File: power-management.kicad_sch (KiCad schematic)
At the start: 11 parts, among them Q1 PMOS, U4 AP2112K-3.3

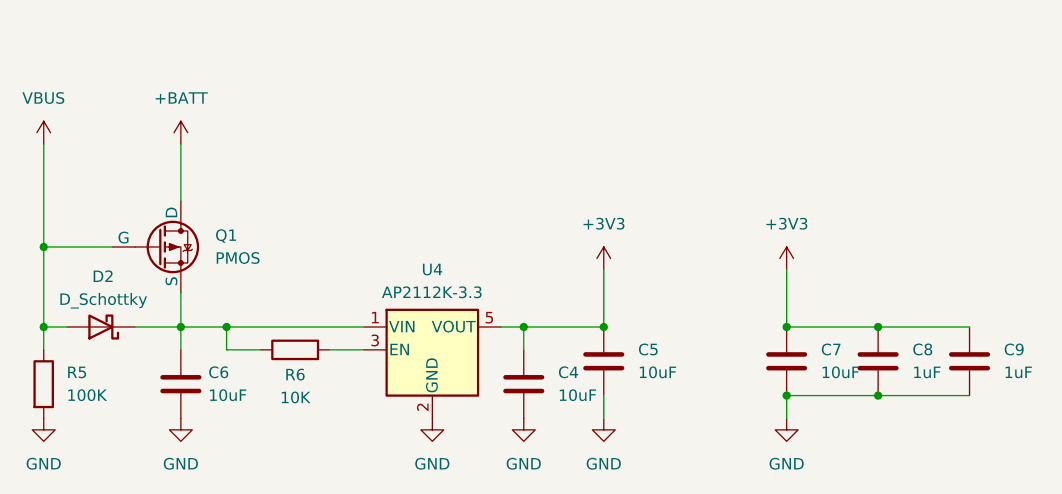
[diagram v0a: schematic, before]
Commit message: Adding symbols information
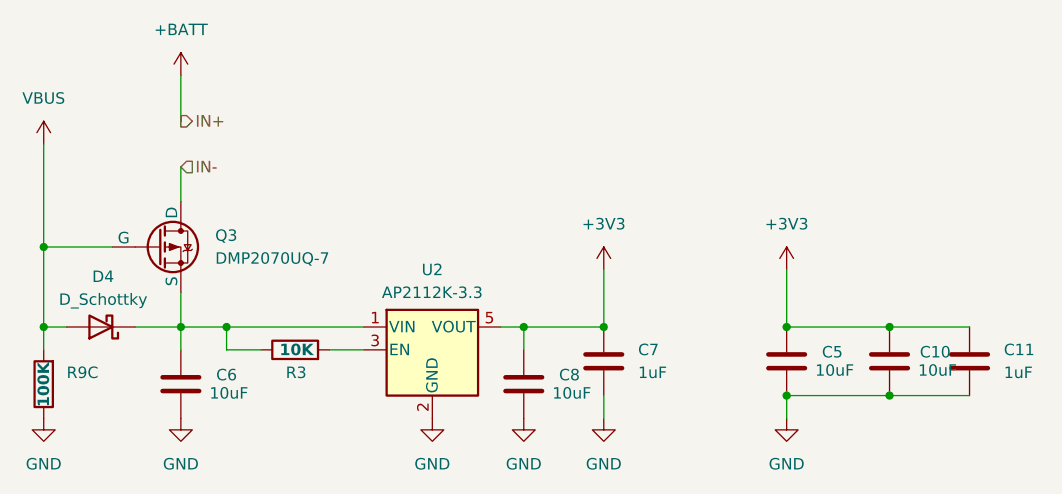
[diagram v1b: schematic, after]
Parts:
- removed C4: 10uF, symbol Device:C
- removed C9: 1uF, symbol Device:C
- removed R5: 100K, symbol Device:R
- removed R6: 10K, symbol Device:R
- added C10: 10uF, Inductor_SMD:L_0805_2012Metric, symbol Device:C
- added C11: 1uF, Capacitor_SMD:C_0603_1608Metric, symbol Device:C
- added R3: 10K, Resistor_SMD:R_0603_1608Metric, symbol Device:R
- added R9C: 100K, Resistor_SMD:R_Array_Convex_4x1206, symbol Device:R
- C5, C6: footprint (none) -> Inductor_SMD:L_0805_2012Metric; Mfr (none) -> Samsung Electro-Mechanics; Mfr P/N (none) -> CL21A106KOQNNNE; Supplier_1 (none) -> Digikey; Supplier_1 P/N (none) -> 1276-1096-1-ND; Supplier_1 Price @ Qty (none) -> 0.03130; Supplier_1 Unit Price (none) -> 0.10
- C7: value 10uF -> 1uF; footprint (none) -> Capacitor_SMD:C_0603_1608Metric; Mfr (none) -> YAGEO; Mfr P/N (none) -> CC0603KRX7R7BB105; Supplier_1 (none) -> Digikey; Supplier_1 P/N (none) -> 0.10; Supplier_1 Unit Price (none) -> 0.03080
- C8: value 1uF -> 10uF; footprint (none) -> Inductor_SMD:L_0805_2012Metric; Mfr (none) -> Samsung Electro-Mechanics; Mfr P/N (none) -> CL21A106KOQNNNE; Supplier_1 (none) -> Digikey; Supplier_1 P/N (none) -> 1276-1096-1-ND; Supplier_1 Price @ Qty (none) -> 0.03130; Supplier_1 Unit Price (none) -> 0.10
- Q3: renamed from Q1; value PMOS -> DMP2070UQ-7; footprint (none) -> Package_TO_SOT_SMD:SOT-23-5_HandSoldering; Mfr (none) -> Diodes Incorporated; Mfr P/N (none) -> DMP2070UQ-7; Supplier_1 (none) -> Digikey; Supplier_1 P/N (none) -> 31-DMP2070UQ-7CT-ND; Supplier_1 Price @ Qty (none) -> 0.1860; Supplier_1 Unit Price (none) -> 0.48
- U2: renamed from U4; Mfr (none) -> Diodes Incorporated; Mfr P/N (none) -> AP2112K-3.3TRG1; Supplier_1 (none) -> Digikey; Supplier_1 P/N (none) -> AP2112K-3.3TRG1DICT-ND; Supplier_1 Price @ Qty (none) -> 0.1955; Supplier_1 Unit Price (none) -> 0.35
- renumbered D2 to D4
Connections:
- net +3V3: now also C10.1, C11.2
- net +BATT: no longer Q3.1 (D)
- net GND: now also C10.2, C11.1, R9C.1
- net VBUS: now also R9C.2
- net at C6.1, D4.1 (K), Q3.3 (S)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: now also R3.1
- net at U2.3 (EN): now also R3.2
- new net IN-: Q3.1 (D)
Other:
- company: (none) -> catbranchman
- title: (none) -> Power - Management

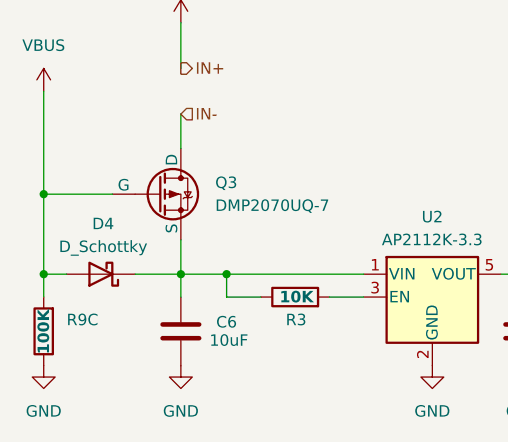
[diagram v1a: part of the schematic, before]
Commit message: Fixing footprint imports
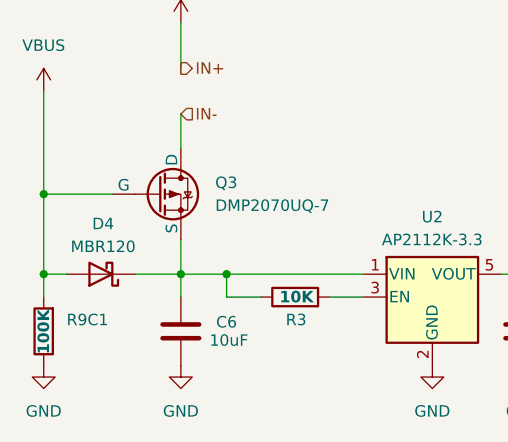
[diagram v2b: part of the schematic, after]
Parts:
- removed R9C: 100K, Resistor_SMD:R_Array_Convex_4x1206, symbol Device:R
- added R9C1: 100K, Resistor_SMD:R_Array_Convex_4x0603, symbol Device:R
- D4: value D_Schottky -> MBR120; footprint (none) -> Diode_SMD:D_SOD-123; Mfr (none) -> onsemi; Mfr P/N (none) -> MBR120LSFT1G; Supplier_1 (none) -> Digikey; Supplier_1 P/N (none) -> MBR120LSFT1GOSCT-ND; Supplier_1 Price @ Qty (none) -> 0.19610; Supplier_1 Unit Price (none) -> 0.42
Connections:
- net GND: now also R9C1.1
- net VBUS: now also R9C1.2
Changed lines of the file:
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@@
 			)
 		)
-		(property "Value" "D_Schottky"
+		(property "Value" "MBR120"
 			(at 87.884 102.362 0)
 			(effects
@@
 			)
 		)
-		(property "Footprint" ""
+		(property "Footprint" "Diode_SMD:D_SOD-123"
 			(at 87.63 105.41 0)
 			(effects
@@
 			)
 		)
-		(property "Datasheet" "~"
+		(property "Datasheet" "https://www.onsemi.com/pdf/datasheet/mbr120lsft1-d.pdf"
 			(at 87.63 105.41 0)
 			(effects
@@
 			)
 		)
-		(property "Description" "Schottky diode"
+		(property "Description" "Diode 20 V 1A Surface Mount SOD-123FL"
+			(at 87.63 105.41 0)
+			(effects
+				(font
+					(size 1.27 1.27)
+				)
+				(hide yes)
+			)
+		)
+		(property "Mfr" "onsemi"
+			(at 87.63 105.41 0)
+			(effects
+				(font
+					(size 1.27 1.27)
+				)
+				(hide yes)
+			)
+		)
+		(property "Mfr P/N" "MBR120LSFT1G"
+			(at 87.63 105.41 0)
+			(effects
+				(font
+					(size 1.27 1.27)
+				)
+				(hide yes)
+			)
+		)
+		(property "Supplier_1" "Digikey"
+			(at 87.63 105.41 0)
+			(effects
+				(font
+					(size 1.27 1.27)
+				)
+				(hide yes)
+			)
+		)
+		(property "Supplier_1 P/N" "MBR120LSFT1GOSCT-ND"
+			(at 87.63 105.41 0)
+			(effects
+				(font
+					(size 1.27 1.27)
+				)
+				(hide yes)
+			)
+		)
+		(property "Supplier_1 Unit Price" "0.42"
+			(at 87.63 105.41 0)
+			(effects
+				(font
+					(size 1.27 1.27)
+				)
+				(hide yes)
+			)
+		)
+		(property "Supplier_1 Price @ Qty" "0.19610"
+			(at 87.63 105.41 0)
+			(effects
+				(font
+					(size 1.27 1.27)
+				)
+				(hide yes)
+			)
+		)
+		(property "Supplier_2" ""
+			(at 87.63 105.41 0)
+			(effects
+				(font
+					(size 1.27 1.27)
+				)
+				(hide yes)
+			)
+		)
+		(property "Supplier_2 P/N" ""
+			(at 87.63 105.41 0)
+			(effects
+				(font
+					(size 1.27 1.27)
+				)
+				(hide yes)
+			)
+		)
+		(property "Supplier_2 Unit Price" ""
+			(at 87.63 105.41 0)
+			(effects
+				(font
+					(size 1.27 1.27)
+				)
+				(hide yes)
+			)
+		)
+		(property "Supplier_2 Price @ Qty" ""
 			(at 87.63 105.41 0)
 			(effects
@@
 	)
 	(symbol
+		(lib_id "Device:R")
+		(at 81.28 111.76 180)
+		(unit 1)
+		(exclude_from_sim no)
+		(in_bom yes)
+		(on_board yes)
+		(dnp no)
+		(property "Reference" "R9C1"
+			(at 83.82 110.4899 0)
+			(effects
+				(font
+					(size 1.27 1.27)
+				)
+				(justify right)
+			)
+		)
+		(property "Value" "100K"
+			(at 81.28 114.3 90)
+			(effects
+				(font
+					(size 1.27 1.27)
+					(thickness 0.254)
+					(bold yes)
+				)
+				(justify right)
+			)
+		)
+		(property "Footprint" "Resistor_SMD:R_Array_Convex_4x0603"
+			(at 83.058 111.76 90)
+			(effects
+				(font
+					(size 1.27 1.27)
+				)
+				(hide yes)
+			)
+		)
+		(property "Datasheet" "https://www.bourns.com/docs/Product-Datasheets/CATCAY.pdf"
+			(at 81.28 111.76 0)
+			(effects
+				(font
+					(size 1.27 1.27)
+				)
+				(hide yes)
+			)
+		)
+		(property "Description" "100k Ohm 1% 62.5mW Power Per Element Isolated 4 Resistor Network/Array 200pm/°C 1206 (3216 Metric), Convex, Long Side Terminals."
+			(at 81.28 111.76 0)
+			(effects
+				(font
+					(size 1.27 1.27)
+				)
+				(hide yes)
+			)
+		)
+		(property "Mfr" "Bourns Inc."
+			(at 81.28 111.76 0)
+			(effects
+				(font
+					(size 1.27 1.27)
+				)
+				(hide yes)
+			)
+		)
+		(property "Mfr P/N" "CAY16-1003F4LF"
+			(at 81.28 111.76 0)
+			(effects
+				(font
+					(size 1.27 1.27)
+				)
+				(hide yes)
+			)
+		)
+		(property "Supplier_1" "Digikey"
+			(at 81.28 111.76 0)
+			(effects
+				(font
+					(size 1.27 1.27)
+				)
+				(hide yes)
+			)
+		)
+		(property "Supplier_1 P/N" "CAY16-1003F4LFCT-ND"
+			(at 81.28 111.76 0)
+			(effects
+				(font
+					(size 1.27 1.27)
+				)
+				(hide yes)
+			)
+		)
+		(property "Supplier_1 Unit Price" "0.10"
+			(at 81.28 111.76 0)
+			(effects
+				(font
+					(size 1.27 1.27)
+				)
+				(hide yes)
+			)
+		)
+		(property "Supplier_1 Price @ Qty" "0.03170"
+			(at 81.28 111.76 0)
+			(effects
+				(font
+					(size 1.27 1.27)
+				)
+				(hide yes)
+			)
+		)
+		(property "Supplier_2" ""
+			(at 81.28 111.76 0)
+			(effects
+				(font
+					(size 1.27 1.27)
+				)
+				(hide yes)
+			)
+		)
+		(property "Supplier_2 P/N" ""
+			(at 81.28 111.76 0)
+			(effects
+				(font
+					(size 1.27 1.27)
+				)
+				(hide yes)
+			)
+		)
+		(property "Supplier_2 Unit Price" ""
+			(at 81.28 111.76 0)
+			(effects
+				(font
+					(size 1.27 1.27)
+				)
+				(hide yes)
+			)
+		)
+		(property "Supplier_2 Price @ Qty" ""
+			(at 81.28 111.76 0)
+			(effects
+				(font
+					(size 1.27 1.27)
+				)
+				(hide yes)
+			)
+		)
+		(pin "2"
+		)
+		(pin "1"
+		)
+		(instances
+			(project "roamer"
+				(path "/1c59de6a-87fe-4223-8898-4b0383164a31/f8947920-db82-4e9f-9d4f-25a180fcfca7"
+					(reference "R9C1")
+					(unit 1)
+				)
+			)
+		)
+	)
+	(symbol
 		(lib_id "Regulator_Linear:AP2112K-3.3")
 		(at 124.46 107.95 0)
@@
 					(unit 1)
 				)
-			)
-		)
-	)
-	(symbol
-		(lib_id "Device:R")
-		(at 81.28 111.76 180)
-		(unit 1)
-		(exclude_from_sim no)
-		(in_bom yes)
-		(on_board yes)
-		(dnp no)
-		(property "Reference" "R9C"
-			(at 83.82 110.4899 0)
-			(effects
-				(font
-					(size 1.27 1.27)
-				)
-				(justify right)
-			)
-		)
-		(property "Value" "100K"
-			(at 81.28 114.3 90)
-			(effects
-				(font
-					(size 1.27 1.27)
-					(thickness 0.254)
-					(bold yes)
-				)
-				(justify right)
-			)
-		)
-		(property "Footprint" "Resistor_SMD:R_Array_Convex_4x1206"
-			(at 83.058 111.76 90)
-			(effects
-				(font
-					(size 1.27 1.27)
-				)
-				(hide yes)
-			)
-		)
-		(property "Datasheet" "https://www.bourns.com/docs/Product-Datasheets/CATCAY.pdf"
-			(at 81.28 111.76 0)
-			(effects
-				(font
-					(size 1.27 1.27)
-				)
-				(hide yes)
-			)
-		)
-		(property "Description" "100k Ohm 1% 62.5mW Power Per Element Isolated 4 Resistor Network/Array 200pm/°C 1206 (3216 Metric), Convex, Long Side Terminals."
-			(at 81.28 111.76 0)
-			(effects
-				(font
-					(size 1.27 1.27)
-				)
-				(hide yes)
-			)
-		)
-		(property "Mfr" "Bourns Inc."
-			(at 81.28 111.76 0)
-			(effects
-				(font
-					(size 1.27 1.27)
-				)
-				(hide yes)
-			)
-		)
-		(property "Mfr P/N" "CAY16-1003F4LF"
-			(at 81.28 111.76 0)
-			(effects
-				(font
-					(size 1.27 1.27)
-				)
-				(hide yes)
-			)
-		)
-		(property "Supplier_1" "Digikey"
-			(at 81.28 111.76 0)
-			(effects
-				(font
-					(size 1.27 1.27)
-				)
-				(hide yes)
-			)
-		)
-		(property "Supplier_1 P/N" "CAY16-1003F4LFCT-ND"
-			(at 81.28 111.76 0)
-			(effects
-				(font
-					(size 1.27 1.27)
-				)
-				(hide yes)
-			)
-		)
-		(property "Supplier_1 Unit Price" "0.10"
-			(at 81.28 111.76 0)
-			(effects
-				(font
-					(size 1.27 1.27)
-				)
-				(hide yes)
-			)
-		)
-		(property "Supplier_1 Price @ Qty" "0.03170"
-			(at 81.28 111.76 0)
-			(effects
-				(font
-					(size 1.27 1.27)
-				)
-				(hide yes)
-			)
-		)
-		(property "Supplier_2" ""
-			(at 81.28 111.76 0)
-			(effects
-				(font
-					(size 1.27 1.27)
-				)
-				(hide yes)
-			)
-		)
-		(property "Supplier_2 P/N" ""
-			(at 81.28 111.76 0)
-			(effects
-				(font
-					(size 1.27 1.27)
-				)
-				(hide yes)
-			)
-		)
-		(property "Supplier_2 Unit Price" ""
-			(at 81.28 111.76 0)
-			(effects
-				(font
-					(size 1.27 1.27)
-				)
-				(hide yes)
-			)
-		)
-		(property "Supplier_2 Price @ Qty" ""
-			(at 81.28 111.76 0)
-			(effects
-				(font
-					(size 1.27 1.27)
-				)
-				(hide yes)
-			)
-		)
-		(pin "2"
-		)
-		(pin "1"
-		)
-		(instances
-			(project "roamer"
-				(path "/1c59de6a-87fe-4223-8898-4b0383164a31/f8947920-db82-4e9f-9d4f-25a180fcfca7"
-					(reference "R9C")
-					(unit 1)
-				)

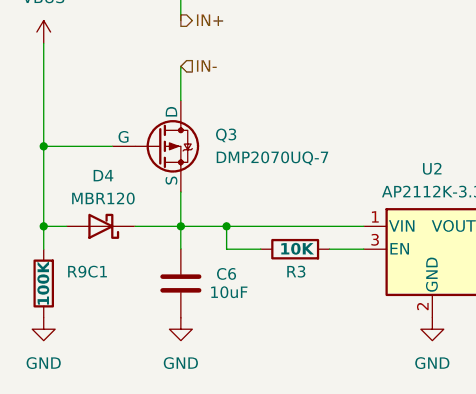
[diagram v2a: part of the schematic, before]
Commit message: Spamming 0 ohm resistors
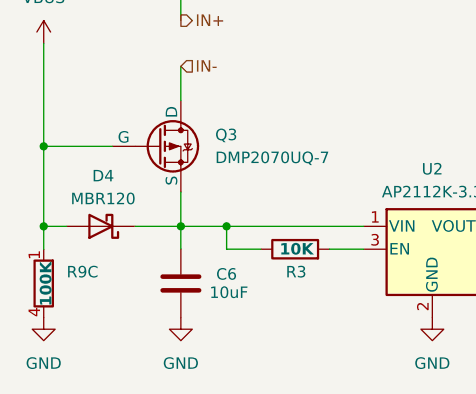
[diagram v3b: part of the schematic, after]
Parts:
- removed R9C1: 100K, Resistor_SMD:R_Array_Convex_4x0603, symbol Device:R
- added R9: 100K, Resistor_SMD:R_Array_Convex_4x1206, symbol Device:R_Network04_Split
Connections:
- net GND: now also R9.4 (R3.2)
- net VBUS: now also R9.1 (R1)
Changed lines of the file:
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@@
+	)
+	(symbol
+		(lib_id "Device:R_Network04_Split")
+		(at 81.28 111.76 0)
+		(unit 3)
+		(exclude_from_sim no)
+		(in_bom yes)
+		(on_board yes)
+		(dnp no)
+		(property "Reference" "R9"
+			(at 83.82 110.4899 0)
+			(effects
+				(font
+					(size 1.27 1.27)
+				)
+				(justify left)
+			)
+		)
+		(property "Value" "100K"
+			(at 81.534 114.3 90)
+			(effects
+				(font
+					(size 1.27 1.27)
+					(thickness 0.254)
+					(bold yes)
+				)
+				(justify left)
+			)
+		)
+		(property "Footprint" "Resistor_SMD:R_Array_Convex_4x1206"
+			(at 79.248 111.76 90)
+			(effects
+				(font
+					(size 1.27 1.27)
+				)
+				(hide yes)
+			)
+		)
+		(property "Datasheet" "https://www.bourns.com/docs/Product-Datasheets/CATCAY.pdf"
+			(at 81.28 111.76 0)
+			(effects
+				(font
+					(size 1.27 1.27)
+				)
+				(hide yes)
+			)
+		)
+		(property "Description" "100k Ohm 1% 62.5mW Power Per Element Isolated 4 Resistor Network/Array 200pm/°C 1206 (3216 Metric), Convex, Long Side Terminals."
+			(at 81.28 111.76 0)
+			(effects
+				(font
+					(size 1.27 1.27)
+				)
+				(hide yes)
+			)
+		)
+		(property "Mfr" "Bourns Inc."
+			(at 81.28 111.76 0)
+			(effects
+				(font
+					(size 1.27 1.27)
+				)
+				(hide yes)
+			)
+		)
+		(property "Mfr P/N" "CAY16-1003F4LF"
+			(at 81.28 111.76 0)
+			(effects
+				(font
+					(size 1.27 1.27)
+				)
+				(hide yes)
+			)
+		)
+		(property "Supplier_1" "Digikey"
+			(at 81.28 111.76 0)
+			(effects
+				(font
+					(size 1.27 1.27)
+				)
+				(hide yes)
+			)
+		)
+		(property "Supplier_1 P/N" "CAY16-1003F4LFCT-ND"
+			(at 81.28 111.76 0)
+			(effects
+				(font
+					(size 1.27 1.27)
+				)
+				(hide yes)
+			)
+		)
+		(property "Supplier_1 Unit Price" "0.10"
+			(at 81.28 111.76 0)
+			(effects
+				(font
+					(size 1.27 1.27)
+				)
+				(hide yes)
+			)
+		)
+		(property "Supplier_1 Price @ Qty" "0.03170"
+			(at 81.28 111.76 0)
+			(effects
+				(font
+					(size 1.27 1.27)
+				)
+				(hide yes)
+			)
+		)
+		(property "Supplier_2" ""
+			(at 81.28 111.76 0)
+			(effects
+				(font
+					(size 1.27 1.27)
+				)
+				(hide yes)
+			)
+		)
+		(property "Supplier_2 P/N" ""
+			(at 81.28 111.76 0)
+			(effects
+				(font
+					(size 1.27 1.27)
+				)
+				(hide yes)
+			)
+		)
+		(property "Supplier_2 Unit Price" ""
+			(at 81.28 111.76 0)
+			(effects
+				(font
+					(size 1.27 1.27)
+				)
+				(hide yes)
+			)
+		)
+		(property "Supplier_2 Price @ Qty" ""
+			(at 81.28 111.76 0)
+			(effects
+				(font
+					(size 1.27 1.27)
+				)
+				(hide yes)
+			)
+		)
+		(pin "2"
+		)
+		(pin "3"
+		)
+		(pin "4"
+		)
+		(pin "5"
+		)
+		(pin "1"
+		)
+		(instances
+			(project "roamer"
+				(path "/1c59de6a-87fe-4223-8898-4b0383164a31/f8947920-db82-4e9f-9d4f-25a180fcfca7"
+					(reference "R9")
+					(unit 3)
+				)
+			)
+		)
 	)
 	(symbol
@@
 					(unit 1)
 				)
-			)
-		)
-	)
-	(symbol
-		(lib_id "Device:R")
-		(at 81.28 111.76 180)
-		(unit 1)
-		(exclude_from_sim no)
-		(in_bom yes)
-		(on_board yes)
-		(dnp no)
-		(property "Reference" "R9C1"
-			(at 83.82 110.4899 0)
-			(effects
-				(font
-					(size 1.27 1.27)
-				)
-				(justify right)
-			)
-		)
-		(property "Value" "100K"
-			(at 81.28 114.3 90)
-			(effects
-				(font
-					(size 1.27 1.27)
-					(thickness 0.254)
-					(bold yes)
-				)
-				(justify right)
-			)
-		)
-		(property "Footprint" "Resistor_SMD:R_Array_Convex_4x0603"
-			(at 83.058 111.76 90)
-			(effects
-				(font
-					(size 1.27 1.27)
-				)
-				(hide yes)
-			)
-		)
-		(property "Datasheet" "https://www.bourns.com/docs/Product-Datasheets/CATCAY.pdf"
-			(at 81.28 111.76 0)
-			(effects
-				(font
-					(size 1.27 1.27)
-				)
-				(hide yes)
-			)
-		)
-		(property "Description" "100k Ohm 1% 62.5mW Power Per Element Isolated 4 Resistor Network/Array 200pm/°C 1206 (3216 Metric), Convex, Long Side Terminals."
-			(at 81.28 111.76 0)
-			(effects
-				(font
-					(size 1.27 1.27)
-				)
-				(hide yes)
-			)
-		)
-		(property "Mfr" "Bourns Inc."
-			(at 81.28 111.76 0)
-			(effects
-				(font
-					(size 1.27 1.27)
-				)
-				(hide yes)
-			)
-		)
-		(property "Mfr P/N" "CAY16-1003F4LF"
-			(at 81.28 111.76 0)
-			(effects
-				(font
-					(size 1.27 1.27)
-				)
-				(hide yes)
-			)
-		)
-		(property "Supplier_1" "Digikey"
-			(at 81.28 111.76 0)
-			(effects
-				(font
-					(size 1.27 1.27)
-				)
-				(hide yes)
-			)
-		)
-		(property "Supplier_1 P/N" "CAY16-1003F4LFCT-ND"
-			(at 81.28 111.76 0)
-			(effects
-				(font
-					(size 1.27 1.27)
-				)
-				(hide yes)
-			)
-		)
-		(property "Supplier_1 Unit Price" "0.10"
-			(at 81.28 111.76 0)
-			(effects
-				(font
-					(size 1.27 1.27)
-				)
-				(hide yes)
-			)
-		)
-		(property "Supplier_1 Price @ Qty" "0.03170"
-			(at 81.28 111.76 0)
-			(effects
-				(font
-					(size 1.27 1.27)
-				)
-				(hide yes)
-			)
-		)
-		(property "Supplier_2" ""
-			(at 81.28 111.76 0)
-			(effects
-				(font
-					(size 1.27 1.27)
-				)
-				(hide yes)
-			)
-		)
-		(property "Supplier_2 P/N" ""
-			(at 81.28 111.76 0)
-			(effects
-				(font
-					(size 1.27 1.27)
-				)
-				(hide yes)
-			)
-		)
-		(property "Supplier_2 Unit Price" ""
-			(at 81.28 111.76 0)
-			(effects
-				(font
-					(size 1.27 1.27)
-				)
-				(hide yes)
-			)
-		)
-		(property "Supplier_2 Price @ Qty" ""
-			(at 81.28 111.76 0)
-			(effects
-				(font
-					(size 1.27 1.27)
-				)
-				(hide yes)
-			)
-		)
-		(pin "2"
-		)
-		(pin "1"
-		)
-		(instances
-			(project "roamer"
-				(path "/1c59de6a-87fe-4223-8898-4b0383164a31/f8947920-db82-4e9f-9d4f-25a180fcfca7"
-					(reference "R9C1")
-					(unit 1)
-				)
